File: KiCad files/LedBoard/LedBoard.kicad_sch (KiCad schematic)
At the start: 19 parts, among them J1 Conn_01x02, J2 Conn_01x02, Q1 IRLR120NTRPBF

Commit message: made some small tweaks
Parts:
- LED1, LED2, LED3: value GW_VJLPL1.CM-K3LX-XX51-1 -> GW VJLPL1.CM-K3LX-XX55-1
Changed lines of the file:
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@@
       (effects (font (size 1.27 1.27)))
     )
-    (property "Value" "GW_VJLPL1.CM-K3LX-XX51-1" (at 74.93 85.09 0)
+    (property "Value" "GW VJLPL1.CM-K3LX-XX55-1" (at 74.93 85.09 0)
       (effects (font (size 1.27 1.27)))
     )
@@
   (symbol (lib_id "GW_VJLPL1.CM-K3LX-XX51-1:GW_VJLPL1.CM-K3LX-XX51-1") (at 82.55 78.105 0) (mirror y) (unit 1)
     (in_bom yes) (on_board yes) (dnp no) (fields_autoplaced)
-    (property "Reference" "LED1" (at 74.93 67.945 0)
-      (effects (font (size 1.27 1.27)))
-    )
-    (property "Value" "GW_VJLPL1.CM-K3LX-XX51-1" (at 74.93 70.485 0)
+    (property "Reference" "LED1" (at 74.93 68.58 0)
+      (effects (font (size 1.27 1.27)))
+    )
+    (property "Value" "GW VJLPL1.CM-K3LX-XX55-1" (at 74.93 71.12 0)
       (effects (font (size 1.27 1.27)))
     )
@@
       (effects (font (size 1.27 1.27)))
     )
-    (property "Value" "GW_VJLPL1.CM-K3LX-XX51-1" (at 74.93 100.33 0)
-      (effects (font (size 1.27 1.27)))
-    )
+    (property "Value" "GW VJLPL1.CM-K3LX-XX55-1" (at 74.93 100.33 0)
+      (effects (font (size 1.27 1.27)))
+    )

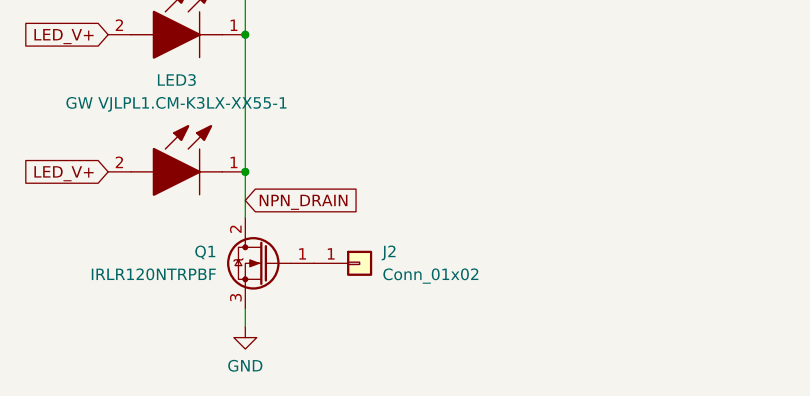
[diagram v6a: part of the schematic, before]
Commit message: modified IO board and LED board so they connect together using XT60
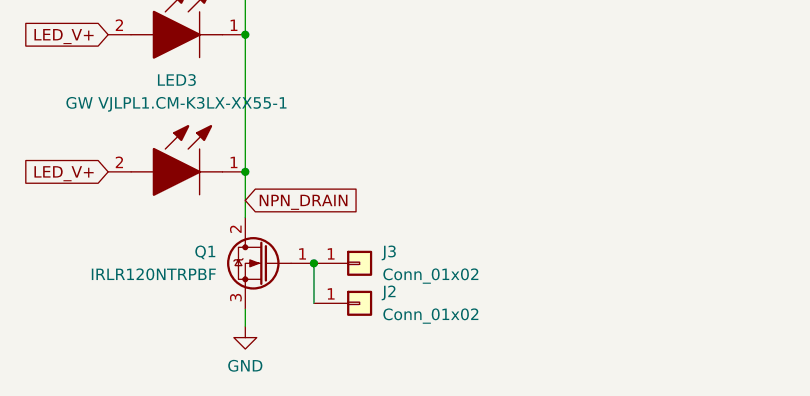
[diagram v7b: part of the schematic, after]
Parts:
- added J3: Conn_01x02, Connector_PinSocket_2.54mm:PinSocket_1x01_P2.54mm_Vertical, symbol Connector_Generic:Conn_01x01
- J1: footprint Connector_Wire:SolderWire-2sqmm_1x02_P7.8mm_D2mm_OD3.9mm -> Connector_AMASS:AMASS_XT60-F_1x02_P7.20mm_Vertical
- J2: footprint Connector_Wire:SolderWire-2sqmm_1x01_D2mm_OD3.9mm -> Connector_PinSocket_2.54mm:PinSocket_1x01_P2.54mm_Vertical
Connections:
- net at J2.1 (Pin_1), Q1.1 (G): now also J3.1 (Pin_1)
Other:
- moved on the sheet: J2
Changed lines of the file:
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@@
   (junction (at 82.55 92.71) (diameter 0) (color 0 0 0 0)
   )
+  (junction (at 90.17 118.11) (diameter 0) (color 0 0 0 0)
+  )
   (junction (at 114.935 41.275) (diameter 0) (color 0 0 0 0)
   )
@@
   )
   (wire (pts (xy 107.95 46.355) (xy 107.95 47.625))
+    (stroke (width 0) (type default))
+  )
+  (wire (pts (xy 90.17 122.555) (xy 90.17 118.11))
     (stroke (width 0) (type default))
   )
@@
     )
   )
+  (symbol (lib_id "Connector_Generic:Conn_01x01") (at 95.25 118.11 0) (unit 1)
+    (in_bom yes) (on_board yes) (dnp no) (fields_autoplaced)
+    (property "Reference" "J3" (at 97.79 116.84 0)
+      (effects (font (size 1.27 1.27)) (justify left))
+    )
+    (property "Value" "Conn_01x02" (at 97.79 119.38 0)
+      (effects (font (size 1.27 1.27)) (justify left))
+    )
+    (property "Footprint" "Connector_PinSocket_2.54mm:PinSocket_1x01_P2.54mm_Vertical" (at 95.25 118.11 0)
+      (effects (font (size 1.27 1.27)) hide)
+    )
+    (property "Datasheet" "~" (at 95.25 118.11 0)
+      (effects (font (size 1.27 1.27)) hide)
+    )
+    (pin "1")
+    (instances
+      (project "LedBoard"
+        (path "/7007eb9b-f827-4e2f-a1f8-279aa4f63030"
+          (reference "J3") (unit 1)
+        )
+      )
+    )
+  )
   (symbol (lib_id "GW_VJLPL1.CM-K3LX-XX51-1:GW_VJLPL1.CM-K3LX-XX51-1") (at 82.55 78.105 0) (mirror y) (unit 1)
     (in_bom yes) (on_board yes) (dnp no) (fields_autoplaced)
@@
     )
   )
-  (symbol (lib_id "Connector_Generic:Conn_01x01") (at 95.25 118.11 0) (unit 1)
-    (in_bom yes) (on_board yes) (dnp no) (fields_autoplaced)
-    (property "Reference" "J2" (at 97.79 116.84 0)
-      (effects (font (size 1.27 1.27)) (justify left))
-    )
-    (property "Value" "Conn_01x02" (at 97.79 119.38 0)
-      (effects (font (size 1.27 1.27)) (justify left))
-    )
-    (property "Footprint" "Connector_Wire:SolderWire-2sqmm_1x01_D2mm_OD3.9mm" (at 95.25 118.11 0)
-      (effects (font (size 1.27 1.27)) hide)
-    )
-    (property "Datasheet" "~" (at 95.25 118.11 0)
+  (symbol (lib_id "Connector_Generic:Conn_01x01") (at 95.25 122.555 0) (unit 1)
+    (in_bom yes) (on_board yes) (dnp no) (fields_autoplaced)
+    (property "Reference" "J2" (at 97.79 121.285 0)
+      (effects (font (size 1.27 1.27)) (justify left))
+    )
+    (property "Value" "Conn_01x02" (at 97.79 123.825 0)
+      (effects (font (size 1.27 1.27)) (justify left))
+    )
+    (property "Footprint" "Connector_PinSocket_2.54mm:PinSocket_1x01_P2.54mm_Vertical" (at 95.25 122.555 0)
+      (effects (font (size 1.27 1.27)) hide)
+    )
+    (property "Datasheet" "~" (at 95.25 122.555 0)
       (effects (font (size 1.27 1.27)) hide)
     )
@@
       (effects (font (size 1.27 1.27)) (justify left))
     )
-    (property "Footprint" "Connector_Wire:SolderWire-2sqmm_1x02_P7.8mm_D2mm_OD3.9mm" (at 141.605 53.975 0)
-      (effects (font (size 1.27 1.27)) hide)
-    )
+    (property "Footprint" "Connector_AMASS:AMASS_XT60-F_1x02_P7.20mm_Vertical" (at 141.605 53.975 0)
+      (effects (font (size 1.27 1.27)) hide)
+    )

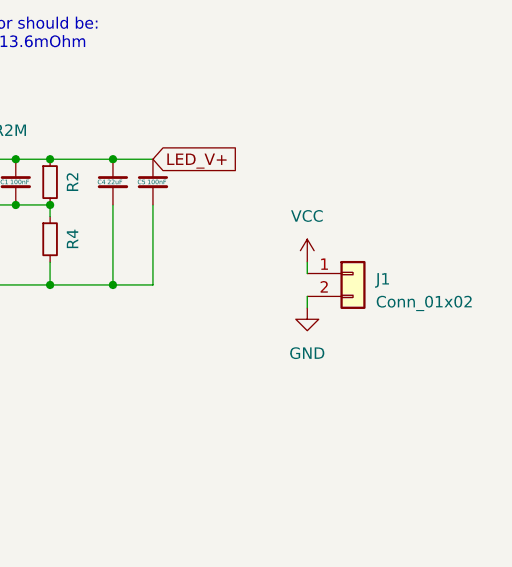
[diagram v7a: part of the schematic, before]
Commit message: corrected VCC and GND being swapped
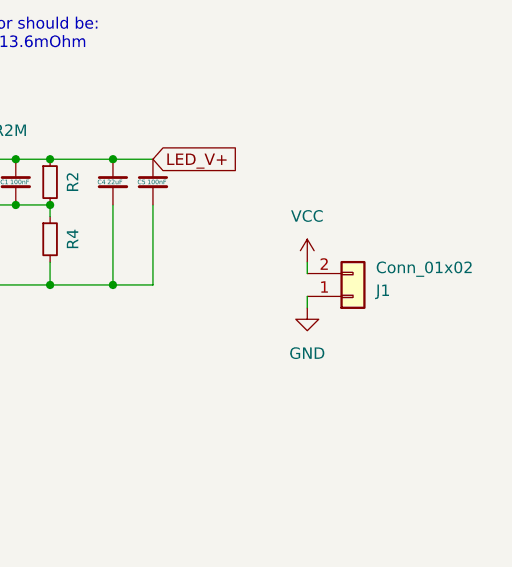
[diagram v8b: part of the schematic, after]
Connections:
- net GND: now also J1.1 (Pin_1); no longer J1.2 (Pin_2)
- net VCC: now also J1.2 (Pin_2); no longer J1.1 (Pin_1)
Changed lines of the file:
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@@
     )
   )
-  (symbol (lib_id "Connector_Generic:Conn_01x02") (at 141.605 53.975 0) (unit 1)
-    (in_bom yes) (on_board yes) (dnp no) (fields_autoplaced)
-    (property "Reference" "J1" (at 144.145 54.61 0)
+  (symbol (lib_id "Connector_Generic:Conn_01x02") (at 141.605 56.515 0) (mirror x) (unit 1)
+    (in_bom yes) (on_board yes) (dnp no)
+    (property "Reference" "J1" (at 144.145 55.88 0)
       (effects (font (size 1.27 1.27)) (justify left))
     )
-    (property "Value" "Conn_01x02" (at 144.145 57.15 0)
+    (property "Value" "Conn_01x02" (at 144.145 53.34 0)
       (effects (font (size 1.27 1.27)) (justify left))
     )
-    (property "Footprint" "Connector_AMASS:AMASS_XT60-F_1x02_P7.20mm_Vertical" (at 141.605 53.975 0)
+    (property "Footprint" "Connector_AMASS:AMASS_XT60-F_1x02_P7.20mm_Vertical" (at 141.605 56.515 0)
       (effects (font (size 1.27 1.27)) hide)
     )
-    (property "Datasheet" "~" (at 141.605 53.975 0)
+    (property "Datasheet" "~" (at 141.605 56.515 0)
       (effects (font (size 1.27 1.27)) hide)
     )
